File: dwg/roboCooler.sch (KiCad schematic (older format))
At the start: 46 parts, among them J1 CONN_02X25, J10 CONN_01X12, J11 CONN_01X12, J12 CONN_01X04, J2 CONN_02X25, J3 CONN_01X04, J4 CONN_01X02, J5 CONN_01X02, J9 CONN_01X06, P1 CONN_01X03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

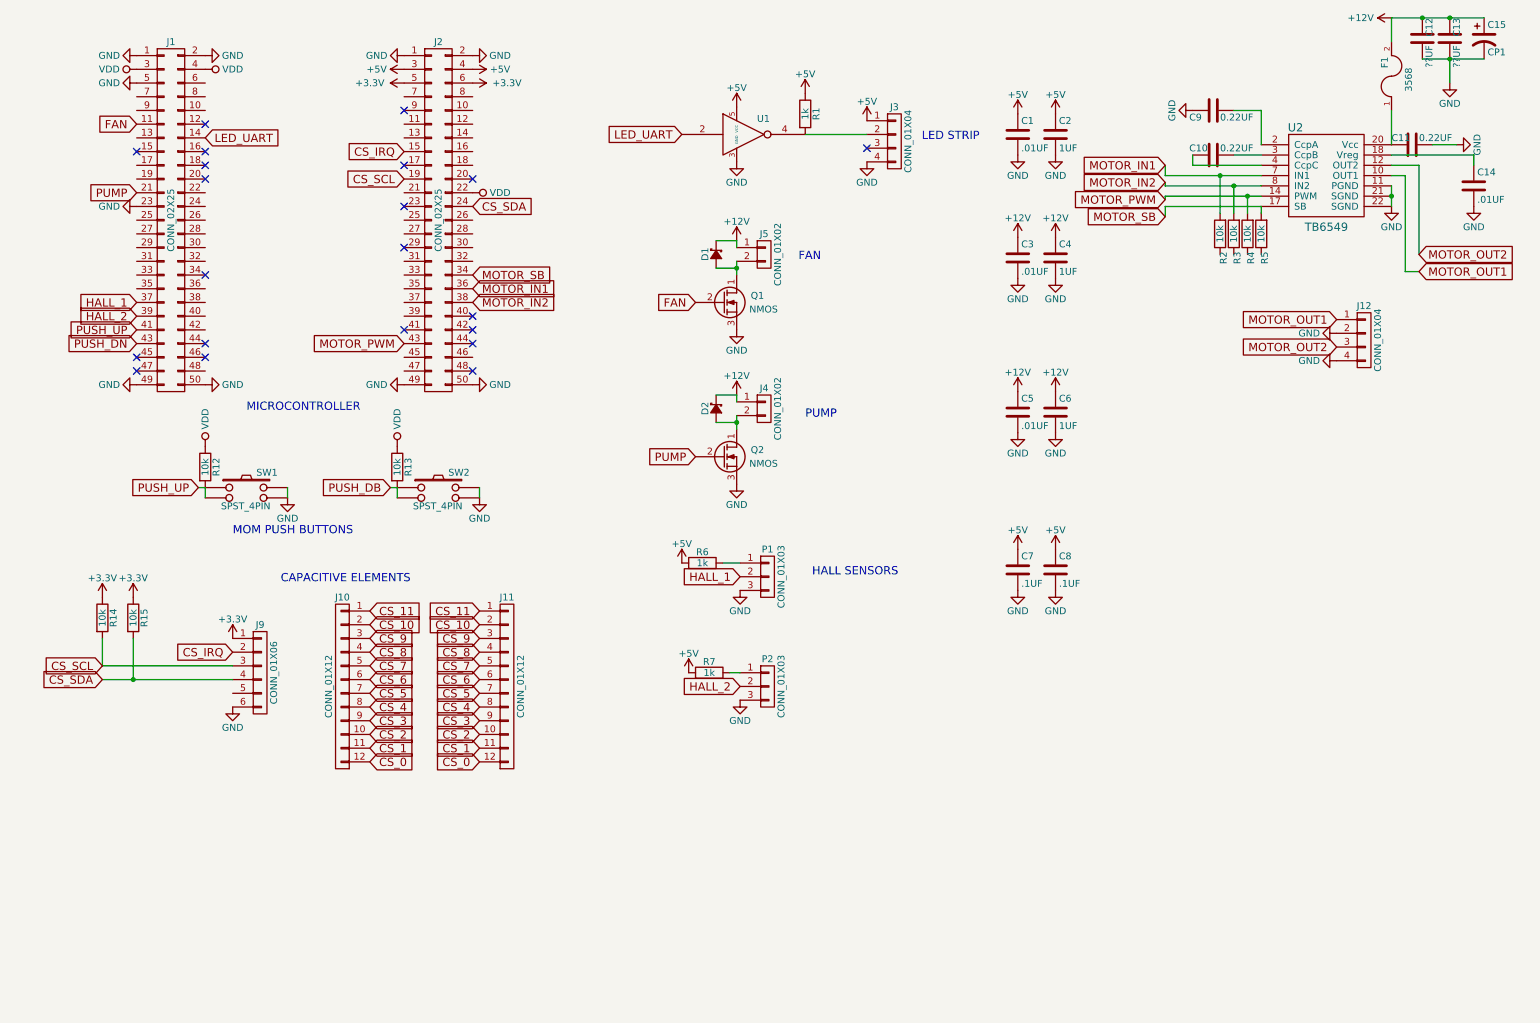
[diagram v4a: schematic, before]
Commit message: updated power nets on schematic
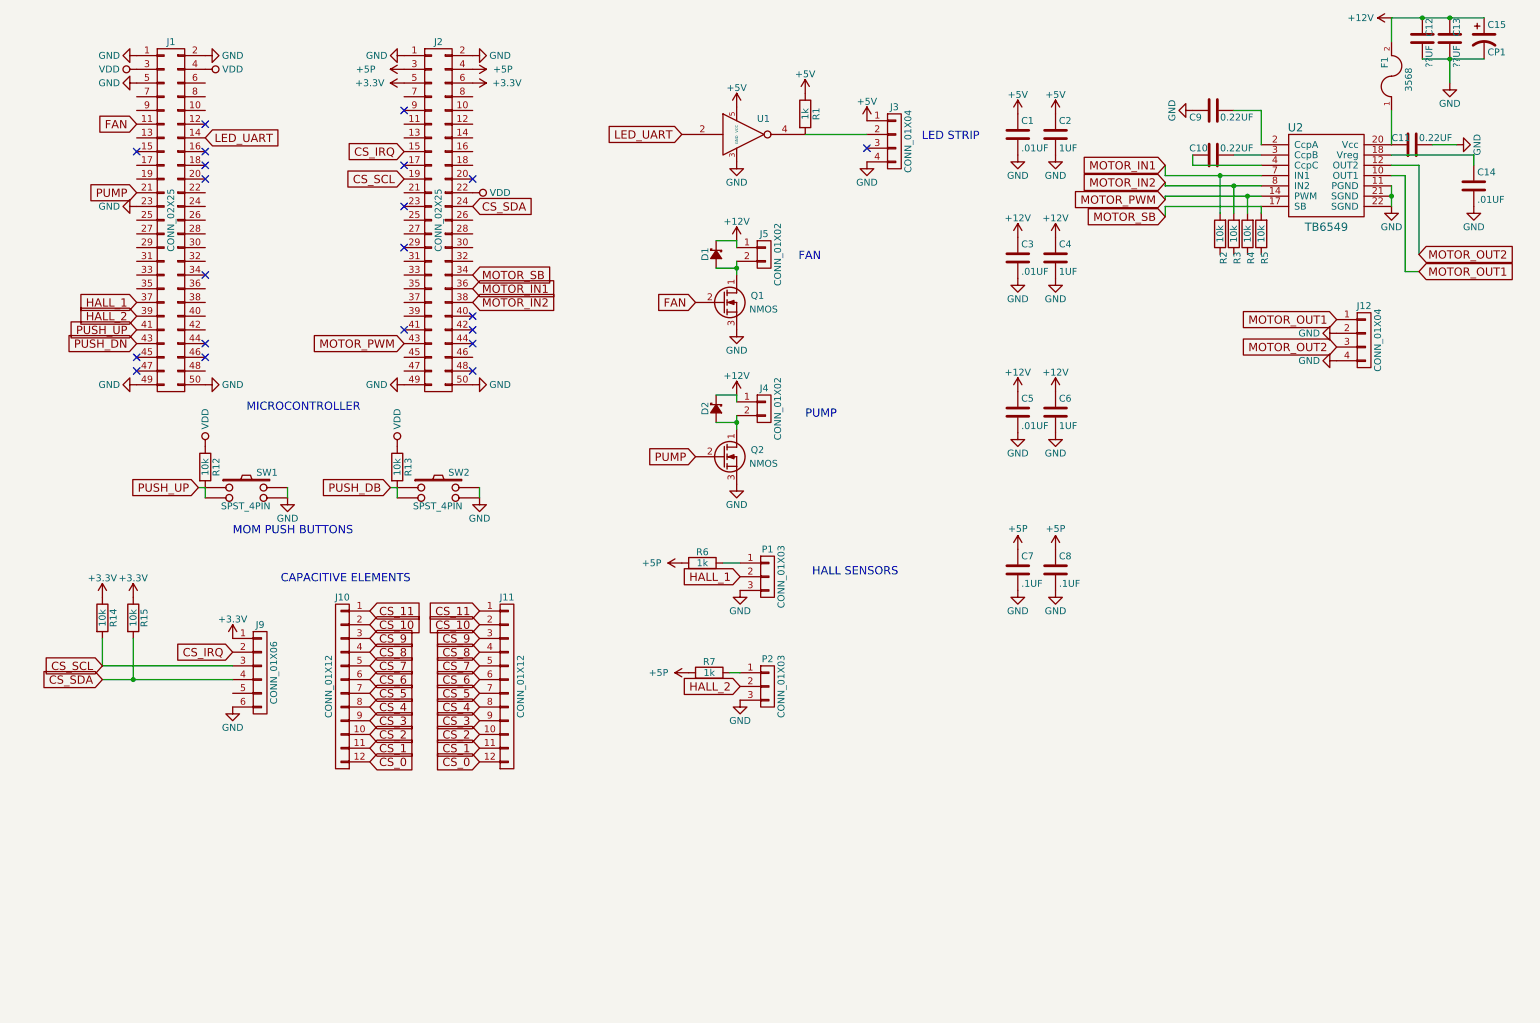
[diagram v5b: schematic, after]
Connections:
- net +5V: no longer C7.1, C8.1, J2.3 (P3), J2.4 (P4), R6.2, R7.2
- new net +5P: C7.1, C8.1, J2.3 (P3), J2.4 (P4), R6.2, R7.2
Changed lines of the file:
@@
-	1    0    0    -1
-$EndComp
-$Comp
-L +5V #PWR26
-U 1 1 566546CD
-P 5175 4500
-F 0 "#PWR26" H 5175 4350 50  0001 C CNN
-F 1 "+5V" H 5175 4640 50  0000 C CNN
-F 2 "" H 5175 4500 60  0000 C CNN
-F 3 "" H 5175 4500 60  0000 C CNN
-	1    5175 4500
 	1    0    0    -1
 $EndComp
@@
 $EndComp
 $Comp
-L +5V #PWR21
-U 1 1 56662DEF
-P 3650 900
-F 0 "#PWR21" H 3650 750 50  0001 C CNN
-F 1 "+5V" V 3650 1100 50  0000 C CNN
-F 2 "" H 3650 900 60  0000 C CNN
-F 3 "" H 3650 900 60  0000 C CNN
-	1    3650 900
-	0    1    1    0
-$EndComp
-$Comp
-L +5V #PWR17
-U 1 1 56662F8C
-P 3150 900
-F 0 "#PWR17" H 3150 750 50  0001 C CNN
-F 1 "+5V" V 3150 1100 50  0000 C CNN
-F 2 "" H 3150 900 60  0000 C CNN
-F 3 "" H 3150 900 60  0000 C CNN
-	1    3150 900
-	0    -1   1    0
-$EndComp
-$Comp
 L VDD #PWR4
 U 1 1 566635F5
@@
 $EndComp
 $Comp
-L +5V #PWR45
-U 1 1 576C6F39
-P 7625 4400
-F 0 "#PWR45" H 7625 4250 50  0001 C CNN
-F 1 "+5V" H 7625 4540 50  0000 C CNN
-F 2 "" H 7625 4400 60  0000 C CNN
-F 3 "" H 7625 4400 60  0000 C CNN
-	1    7625 4400
-	1    0    0    -1
-$EndComp
-$Comp
-L +5V #PWR53
-U 1 1 576C740D
-P 7900 4400
-F 0 "#PWR53" H 7900 4250 50  0001 C CNN
-F 1 "+5V" H 7900 4540 50  0000 C CNN
-F 2 "" H 7900 4400 60  0000 C CNN
-F 3 "" H 7900 4400 60  0000 C CNN
-	1    7900 4400
-	1    0    0    -1
-$EndComp
-$Comp
 L GND #PWR35
 U 1 1 576C7ABC
@@
 F 3 "" H 5600 5500 60  0000 C CNN
 	1    5600 5500
-	1    0    0    -1
-$EndComp
-$Comp
-L +5V #PWR27
-U 1 1 576C7AC2
-P 5225 5300
-F 0 "#PWR27" H 5225 5150 50  0001 C CNN
-F 1 "+5V" H 5225 5440 50  0000 C CNN
-F 2 "" H 5225 5300 60  0000 C CNN
-F 3 "" H 5225 5300 60  0000 C CNN
-	1    5225 5300
 	1    0    0    -1
 $EndComp
@@
 $EndComp
 Wire Wire Line
-	5575 2300 5575 2400
+	5575 2300 5575 2350
+Wire Wire Line
+	5575 2350 5575 2400
 Wire Wire Line
 	5425 2150 5575 2150
@@
 	950  5250 1900 5250
 Wire Wire Line
-	950  5350 1900 5350
+	950  5350 1175 5350
+Wire Wire Line
+	1175 5350 1900 5350
 Wire Wire Line
 	1175 5050 1175 5350
 Connection ~ 1175 5350
 Wire Wire Line
-	5575 3425 5575 3525
+	5575 3425 5575 3475
+Wire Wire Line
+	5575 3475 5575 3525
 Wire Wire Line
 	5425 3275 5575 3275
@@
 	5575 3275 5575 3325
 Wire Wire Line
-	10350 1750 10350 1900
+	10350 1750 10350 1825
+Wire Wire Line
+	10350 1825 10350 1900
 Wire Wire Line
 	9400 1525 9200 1525
@@
 	10350 1200 10350 1450
 Wire Wire Line
-	10575 825  11025 825
+	10575 825  10775 825
+Wire Wire Line
+	10775 825  11025 825
 Wire Wire Line
 	10775 1000 10775 825
@@
 $EndComp
 Wire Wire Line
-	8700 1675 9400 1675
+	8700 1675 9100 1675
+Wire Wire Line
+	9100 1675 9400 1675
 $Comp
 L R R4
@@
 $EndComp
 Wire Wire Line
-	8700 1825 9400 1825
+	8700 1825 9300 1825
+Wire Wire Line
+	9300 1825 9400 1825
 Wire Wire Line
 	9300 1825 9300 1950
@@
 $EndComp
 Wire Wire Line
-	8700 1750 9400 1750
+	8700 1750 9200 1750
+Wire Wire Line
+	9200 1750 9400 1750
 Wire Wire Line
 	9200 1750 9200 1950
@@
 MOTOR_SB
 Wire Wire Line
-	10350 525  11025 525
+	10350 525  10575 525
+Wire Wire Line
+	10575 525  10775 525
+Wire Wire Line
+	10775 525  11025 525
 Connection ~ 10775 525
 Connection ~ 10575 525
@@
 Wire Wire Line
 	5525 5300 5600 5300
+$Comp
+L +5P #PWR?
+U 1 1 577BAD0E
+P 3150 900
+F 0 "#PWR?" H 3150 750 50  0001 C CNN
+F 1 "+5P" V 3150 1180 50  0000 C CNN
+F 2 "" H 3150 900 50  0000 C CNN
+F 3 "" H 3150 900 50  0000 C CNN
+	1    3150 900
+	0    -1   -1   0
+$EndComp
+$Comp
+L +5P #PWR?
+U 1 1 577BB694
+P 3650 900
+F 0 "#PWR?" H 3650 750 50  0001 C CNN
+F 1 "+5P" V 3650 1120 50  0000 C CNN
+F 2 "" H 3650 900 50  0000 C CNN
+F 3 "" H 3650 900 50  0000 C CNN
+	1    3650 900
+	0    1    -1   0
+$EndComp
+$Comp
+L +5P #PWR?
+U 1 1 577BCEFC
+P 5175 4500
+F 0 "#PWR?" H 5175 4350 50  0001 C CNN
+F 1 "+5P" V 5175 4720 50  0000 C CNN
+F 2 "" H 5175 4500 50  0000 C CNN
+F 3 "" H 5175 4500 50  0000 C CNN
+	1    5175 4500
+	0    -1   1    0
+$EndComp
+$Comp
+L +5P #PWR?
+U 1 1 577C06F6
+P 5225 5300
+F 0 "#PWR?" H 5225 5150 50  0001 C CNN
+F 1 "+5P" V 5225 5520 50  0000 C CNN
+F 2 "" H 5225 5300 50  0000 C CNN
+F 3 "" H 5225 5300 50  0000 C CNN
+	1    5225 5300
+	0    -1   1    0
+$EndComp
+$Comp
+L +5P #PWR?
+U 1 1 577C142C
+P 7625 4400
+F 0 "#PWR?" H 7625 4250 50  0001 C CNN
+F 1 "+5P" H 7625 4550 50  0000 C CNN
+F 2 "" H 7625 4400 50  0000 C CNN
+F 3 "" H 7625 4400 50  0000 C CNN
+	1    7625 4400
+	-1   0    0    -1
+$EndComp
+$Comp
+L +5P #PWR?
+U 1 1 577C1D66
+P 7900 4400
+F 0 "#PWR?" H 7900 4250 50  0001 C CNN
+F 1 "+5P" H 7900 4550 50  0000 C CNN
+F 2 "" H 7900 4400 50  0000 C CNN
+F 3 "" H 7900 4400 50  0000 C CNN
+	1    7900 4400
+	-1   0    0    -1
+$EndComp
 $EndSCHEMATC

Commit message: updated power entery to baord
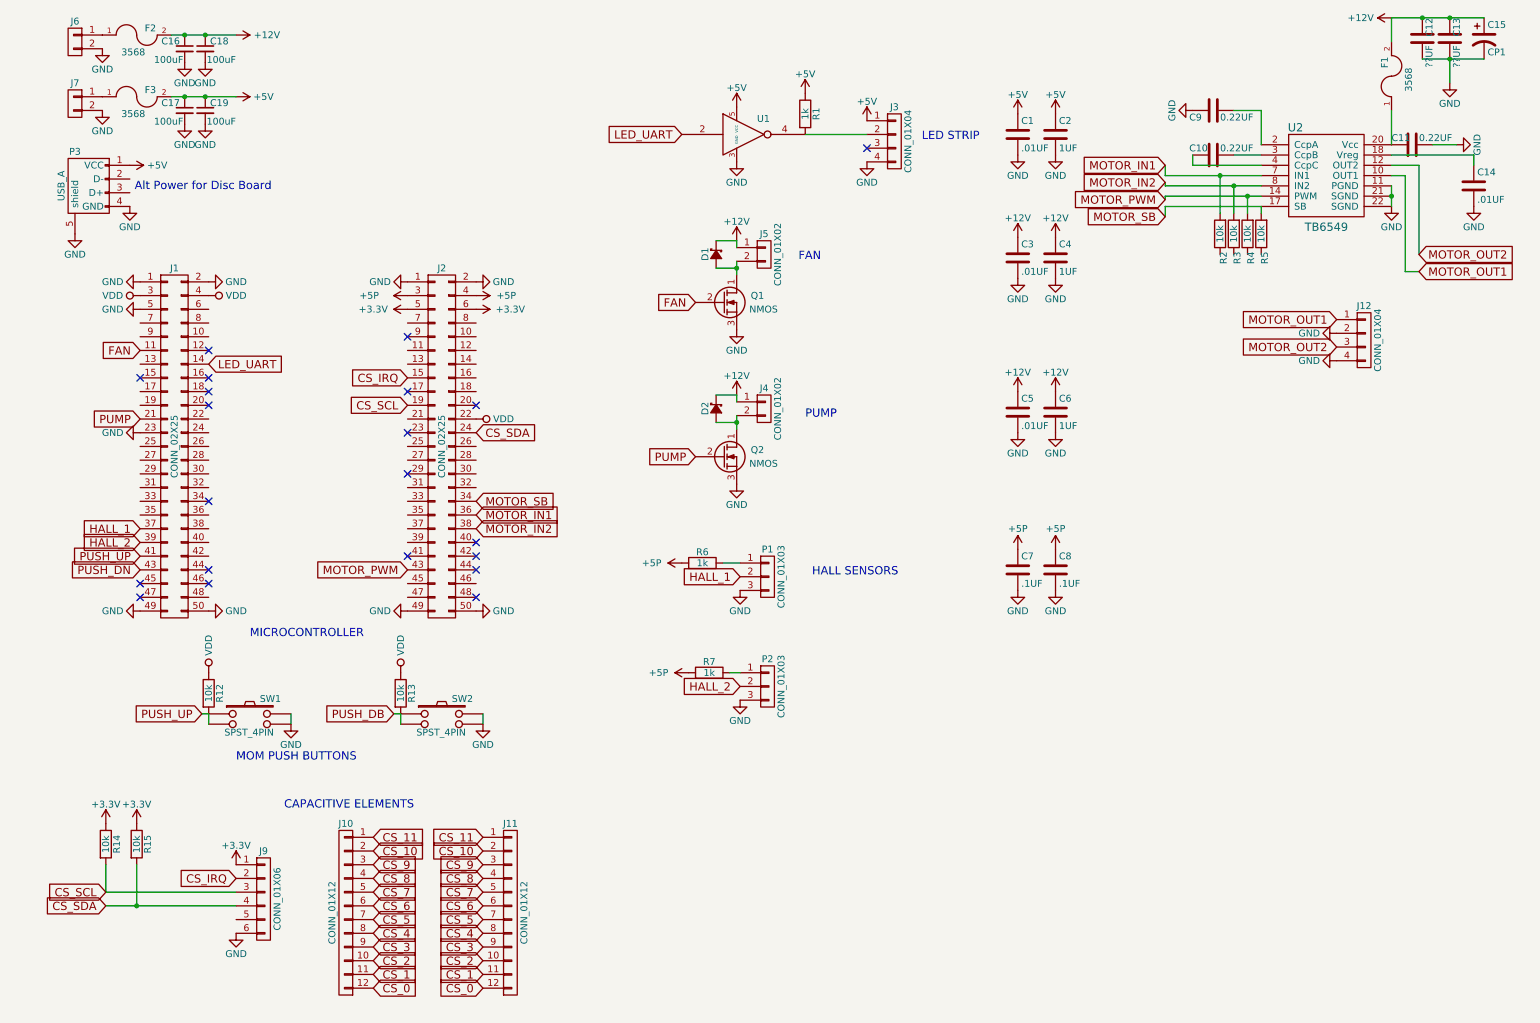
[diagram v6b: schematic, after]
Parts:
- added C16, C17, C18, C19: 100uF, symbol C_Small
- added F2, F3: 3568, roboCooler:3568, symbol FUSE
- added J6, J7: CONN_01X02, symbol CONN_01X02
- added P3: USB_A, symbol USB_A
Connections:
- net +12V: now also C16.1, C18.1, F2.2
- net +5V: now also C17.1, C19.1, F3.2, P3.1 (VCC)
- net GND: now also C16.2, C17.2, C18.2, C19.2, J6.2 (P2), J7.2 (P2), P3.4 (GND), P3.5 (shield)
- new net: F2.1, J6.1 (P1)
- new net: F3.1, J7.1 (P1)
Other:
- note added: "Alt Power for Disc Board"
- moved on the sheet: J1, J10, J11, J2, J9, R12, R13, R14, R15, SW1, SW2

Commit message: updated crossbar and no-connects
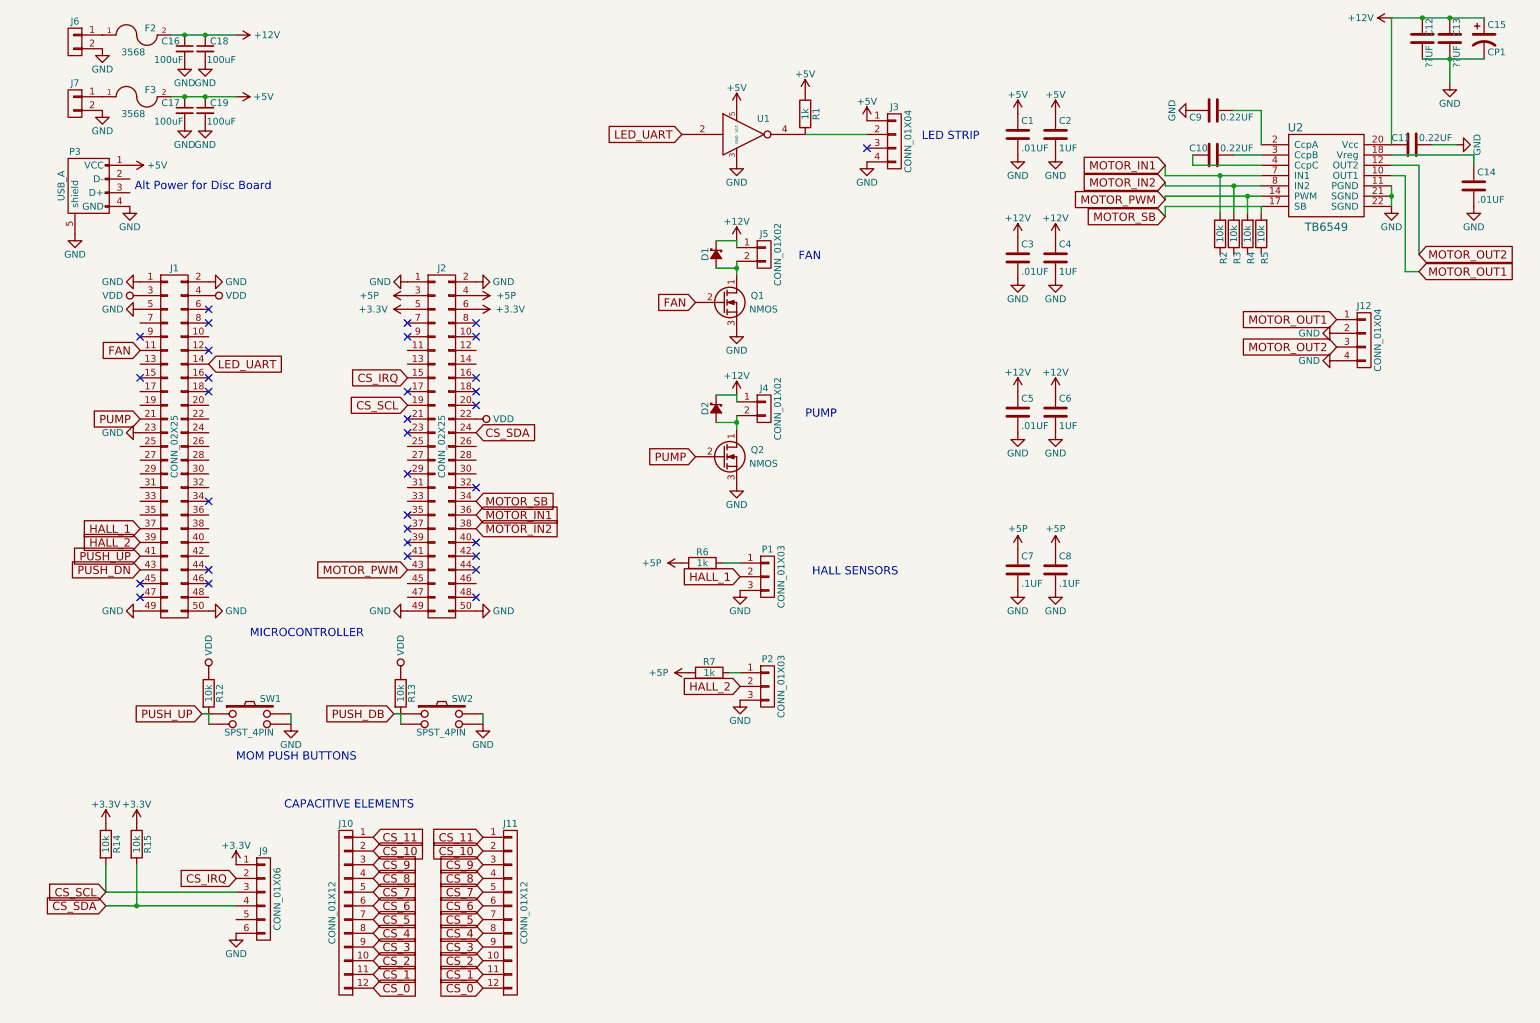
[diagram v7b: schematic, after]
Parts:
- removed F1: 3568, roboCooler:3568, symbol FUSE
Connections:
- net +12V: now also C11.2, U2.20 (Vcc)
- no-connect marks 21 -> 33
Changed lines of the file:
@@
 NoConn ~ 1725 3150
 NoConn ~ 1725 3250
-NoConn ~ 1725 3350
 NoConn ~ 1725 4050
 NoConn ~ 1725 4550
@@
 $EndComp
 $Comp
-L FUSE F1
-U 1 1 5773EC86
-P 10350 950
-F 0 "F1" H 10450 1000 50  0000 C CNN
-F 1 "3568" H 10325 825 50  0000 C CNN
-F 2 "roboCooler:3568" H 10350 950 50  0001 C CNN
-F 3 "" H 10350 950 50  0000 C CNN
-	1    10350 950
-	0    -1   -1   0
-$EndComp
-$Comp
 L C C13
 U 1 1 5774022B
@@
 	9400 1200 9200 1200
 Wire Wire Line
-	10350 1200 10350 1450
+	10350 525  10350 1450
 Wire Wire Line
 	10575 825  11025 825
@@
 	10775 1000 10775 825
 Connection ~ 10775 825
-Wire Wire Line
-	10350 700  10350 525
 Wire Wire Line
 	10650 1450 10825 1450
@@
 Text Notes 1185 1790 0    60   ~ 0
 Alt Power for Disc Board
+NoConn ~ 1725 2650
+NoConn ~ 1725 2750
+NoConn ~ 1225 2850
+NoConn ~ 3175 2750
+NoConn ~ 3675 2750
+NoConn ~ 3675 2850
+NoConn ~ 3675 3150
+NoConn ~ 3675 3250
+NoConn ~ 3175 3450
+NoConn ~ 3675 3950
+NoConn ~ 3175 4150
+NoConn ~ 3175 4250
+NoConn ~ 3175 4350
 $EndSCHEMATC

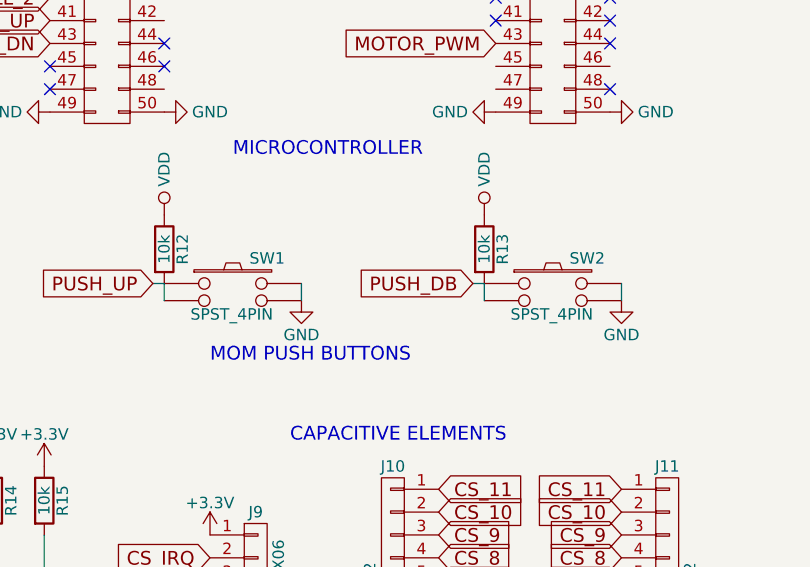
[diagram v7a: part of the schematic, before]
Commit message: synced crossbar with mcu pinout on schematic
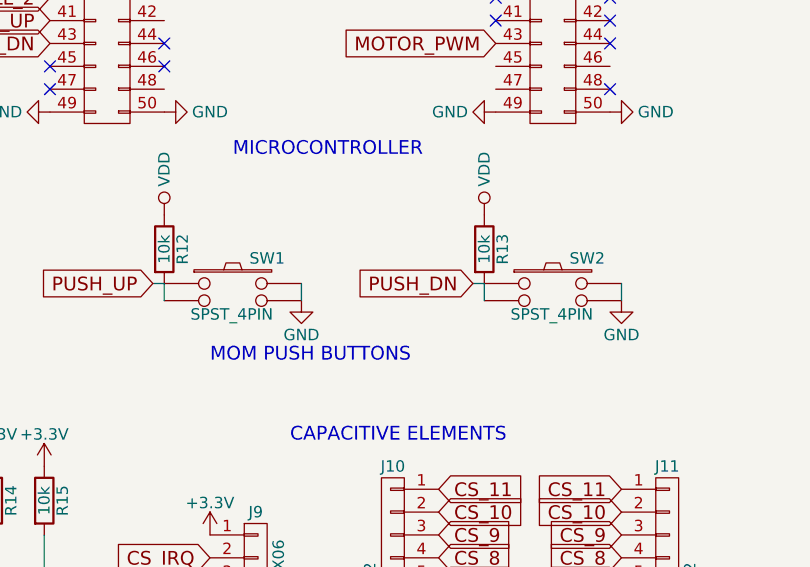
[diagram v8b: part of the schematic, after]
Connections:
- net PUSH_DB is gone; now on net PUSH_DN: R13.2, SW2.1 (C1), SW2.2 (C2)
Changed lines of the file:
@@
 $EndComp
 Text GLabel 3075 5600 0    60   Input ~ 0
-PUSH_DB
+PUSH_DN
 $Comp
 L R R13
